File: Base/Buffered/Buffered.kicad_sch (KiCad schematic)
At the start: 29 parts, among them J1 Barrel_Jack_Switch, J2 Conn_01x04_Pin, J3 Conn_01x04_Pin, J4 AudioJack2_Ground, J5 AudioJack2_Ground, Q2 40V, SW1 SW_Push, U1 LT3462A

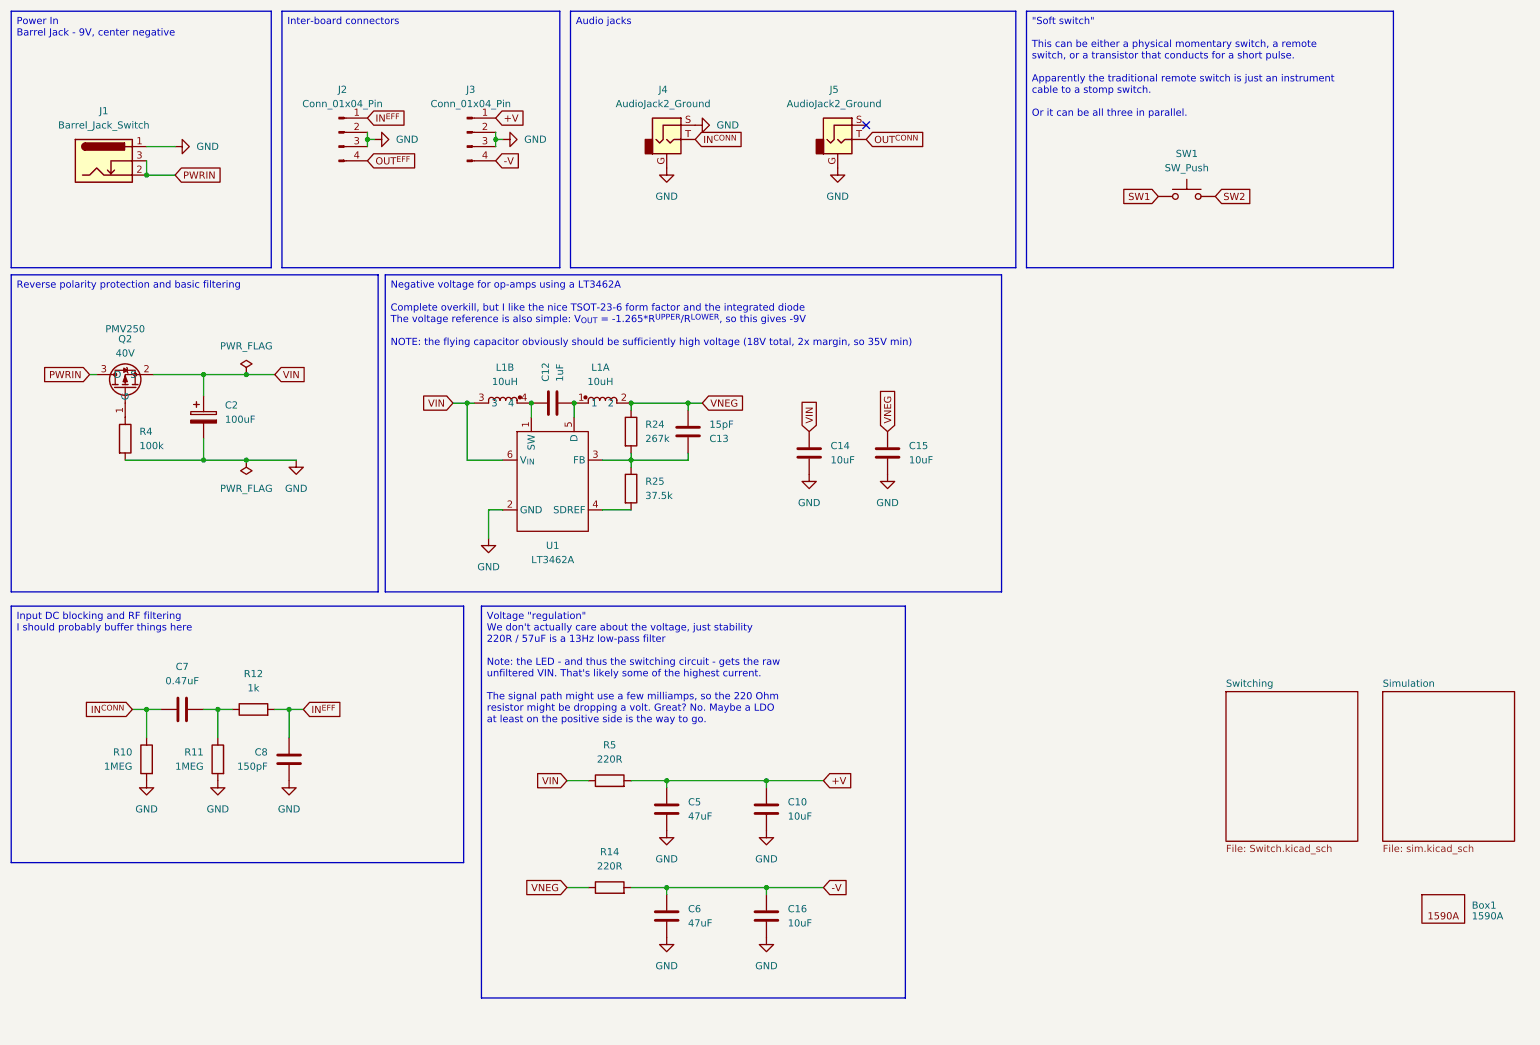
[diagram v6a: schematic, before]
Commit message: Try LDO for positive voltage rail cleaning
As mentioned, I don't think I'll actually build this, because it seems
pointlessly complicated.  But I did the basic design and layout for it
just in case.

I think I'll go back to the single-rail design and keep the MOSFET
switching.

I also think I need to come up with a new project.  I'm kind of running
out of ideas of small projects to do that I can build and test.  I like
the switching circuit, but I'm losing interest in the effects board side
since I still can't actually play guitar.

Signed-off-by: Linus Torvalds <torvalds@linux-foundation.org>
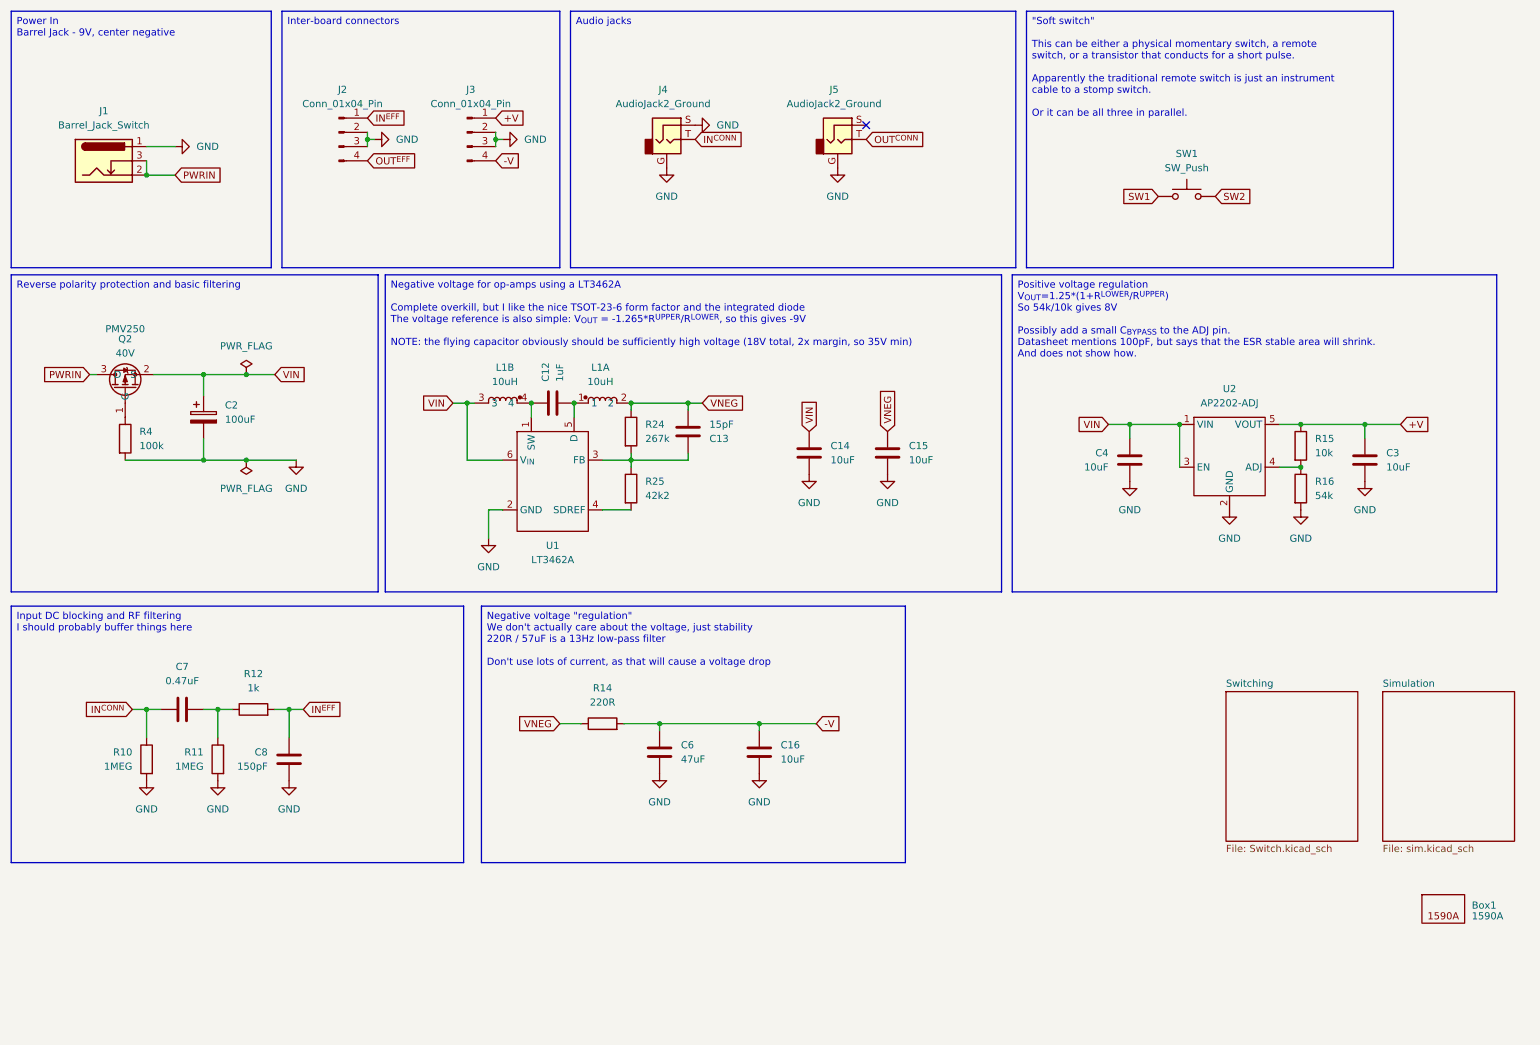
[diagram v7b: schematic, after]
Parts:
- removed C10: 10uF, Capacitor_SMD:C_1206_3216Metric, symbol Device:C
- removed C5: 47uF, Capacitor_SMD:C_1206_3216Metric, symbol Device:C
- removed R5: 220R, Resistor_SMD:R_0805_2012Metric, symbol Device:R
- added C3, C4: 10uF, Capacitor_SMD:C_1206_3216Metric, symbol Device:C
- added R15: 10k, Resistor_SMD:R_0805_2012Metric, symbol Device:R
- added R16: 54k, Resistor_SMD:R_0805_2012Metric, symbol Device:R
- added U2: AP2202-ADJ, Package_TO_SOT_SMD:SOT-23-5, symbol Mylib:AP2202-ADJ
- R25: value 37.5k -> 42k2
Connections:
- net +V: now also C3.1, R15.1, U2.5 (VOUT)
- net GND: now also C3.2, C4.2, R16.2, U2.2 (GND)
- net VIN: now also C4.1, U2.1 (VIN), U2.3 (EN)
- new net: R15.2, R16.1, U2.4 (ADJ)
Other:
- moved on the sheet: C16, C6, R14
